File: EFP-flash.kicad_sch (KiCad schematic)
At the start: 17 parts, among them J101 USB_C_Receptacle_USB2.0, J102 Conn_01x06, Q101 MMDT3904, SW101 SW_SPDT, U101 ESD PROTECTION, U102 TLV75533PDBV, U103 CH340C

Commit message: PCB complete
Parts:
- added D102: GREEN, LED_SMD:LED_0603_1608Metric, symbol Device:LED
- added J101: USB_B_Micro, Connector_USB_custom:USB_Micro-B_Amphenol_10118194_Horizontal, symbol Connector:USB_B_Micro
- added LOGO101: Open_Hardware, Symbol:OSHW-Logo2_7.3x6mm_SilkScreen, symbol Graphic:Logo_Open_Hardware_Large
- added R105: 10kΩ, Resistor_SMD:R_0603_1608Metric, symbol Device:R_Small_US
- J103: renamed from J102; JLCPCB_IGNORE (none) -> 1
- U101: JLCPCB_CORRECTION (none) -> 0;0;180
- U102: JLCPCB_CORRECTION (none) -> 0;0;180; LCSC C255621 C404027 -> C404027
- renumbered J101 to J102
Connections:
- net 3v3_{SW}: now also D102.2 (A)
- net GND: now also J101.5 (GND), J101.6 (Shield), R105.2
- net SER_RX: now also J103.2 (Pin_2); no longer J103.3 (Pin_3)
- net SER_TX: now also J103.3 (Pin_3); no longer J103.2 (Pin_2)
- net USB_D+: now also U101.1 (I/O1), J101.3 (D+); no longer U101.6 (I/O4)
- net USB_D-: now also U101.6 (I/O4), J101.2 (D-); no longer U101.1 (I/O1)
- net at F101.2, J102.A4 (VBUS), J102.A9 (VBUS)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: now also J101.1 (VBUS)
- new net: D102.1 (K), R105.1
- no-connect marks 10 -> 11
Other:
- note added: "Gnd Rx Tx 3v3 EN Boot"
- note removed: "Gnd Tx Rx 3v3 EN Boot"
- moved on the sheet: SW101

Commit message: Sent to board fab v1.0.1, replaces previous
Changes:
 - USB diodes out of stock; different manufacturer had their stock.
 - SPDT switch out of stock, replaced with a different switch that
   thankfully also had a footprint in KiCAD
 - Made the board slightly wider to accomodate the switch.
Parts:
- SW101: footprint Button_Switch_SMD:SW_SPDT_PCM12 -> Button_Switch_SMD:SW_SPDT_CK-JS102011SAQN; JLCPCB_CORRECTION (none) -> 0;-2.75;180; LCSC C109335 -> C125040
- U102: LCSC C404027 -> C2937042
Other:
- company: (none) -> OSH
- title: (none) -> ESP-Flash
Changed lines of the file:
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@@
 (kicad_sch (version 20211123) (generator eeschema)
   (paper "A4")
+  (title_block
+    (title "ESP-Flash")
+    (date "2023-01-03")
+    (rev "v1.1.0")
+    (company "OSH")
+    (comment 1 "Drawn by: VGD")
+  )
   (junction (at 82.55 101.6) (diameter 0) (color 0 0 0 0)
   )
@@
       (effects (font (size 1.27 1.27)) hide)
     )
+    (pin "1")
+    (pin "2")
+    (pin "6")
     (pin "3")
     (pin "4")
@@
     (property "Reference" "SW101" (id 0) (at 213.36 64.77 0))
     (property "Value" "SW_SPDT" (id 1) (at 213.36 67.31 0))
-    (property "Footprint" "Button_Switch_SMD:SW_SPDT_PCM12" (id 2) (at 213.36 72.39 0)
+    (property "Footprint" "Button_Switch_SMD:SW_SPDT_CK-JS102011SAQN" (id 2) (at 213.36 72.39 0)
       (effects (font (size 1.27 1.27)) hide)
     )
@@
       (effects (font (size 1.27 1.27)) hide)
     )
-    (property "LCSC" "C109335" (id 4) (at 213.36 72.39 0)
+    (property "LCSC" "C125040" (id 4) (at 213.36 72.39 0)
+      (effects (font (size 1.27 1.27)) hide)
+    )
+    (property "JLCPCB_CORRECTION" "0;-2.75;180" (id 5) (at 213.36 72.39 0)
       (effects (font (size 1.27 1.27)) hide)
     )
@@
     (pin "2")
     (pin "6")
+    (pin "3")
+    (pin "4")
+    (pin "5")
   )
   (symbol (lib_id "Device:R_US") (at 71.12 113.03 180) (unit 1)
@@
       (effects (font (size 1.27 1.27)) hide)
     )
-    (property "LCSC" "C404027" (id 4) (at 115.57 40.64 0)
+    (property "LCSC" "C2937042" (id 4) (at 115.57 40.64 0)
       (effects (font (size 1.27 1.27)) hide)
     )
@@
     )
     (path "/7fed758a-c76e-4f1a-8799-89d9d2a905c1"
-      (reference "SW101") (unit 1) (value "SW_SPDT") (footprint "Button_Switch_SMD:SW_SPDT_PCM12")
+      (reference "SW101") (unit 1) (value "SW_SPDT") (footprint "Button_Switch_SMD:SW_SPDT_CK-JS102011SAQN")
     )
     (path "/e1bad162-1779-40d0-8d1a-a95bb6a2350e"

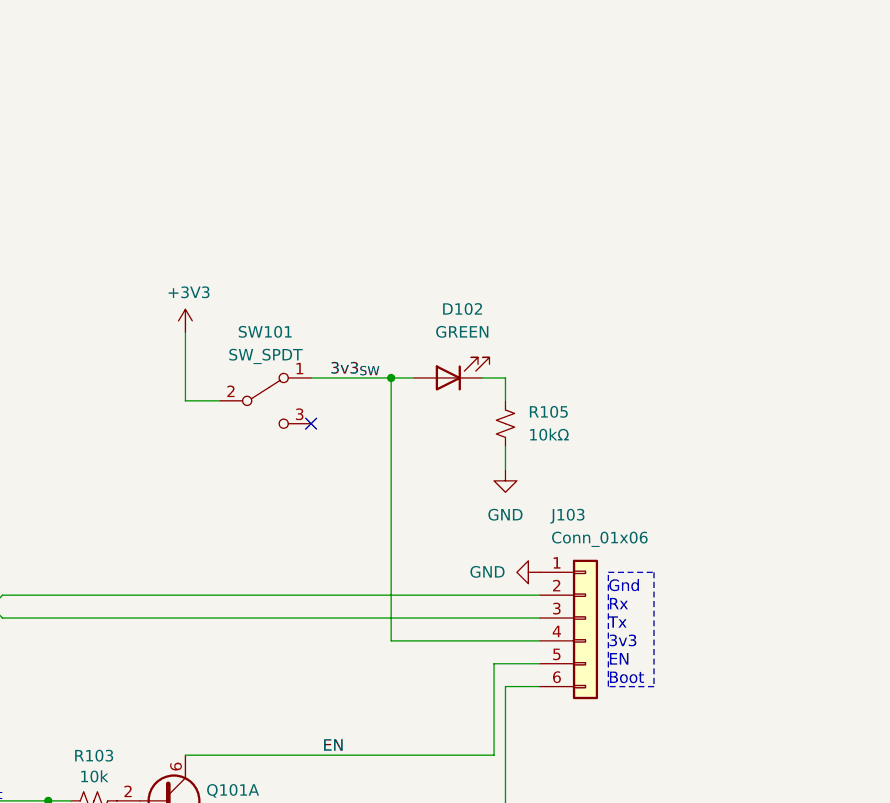
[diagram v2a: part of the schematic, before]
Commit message: Bugfix: PWR LED backfed from board
Power LED would light up when board was using its own 3v3 Power, even
though the switch was in the off position.

Found a clever solution to fix this, by changing two short traces.
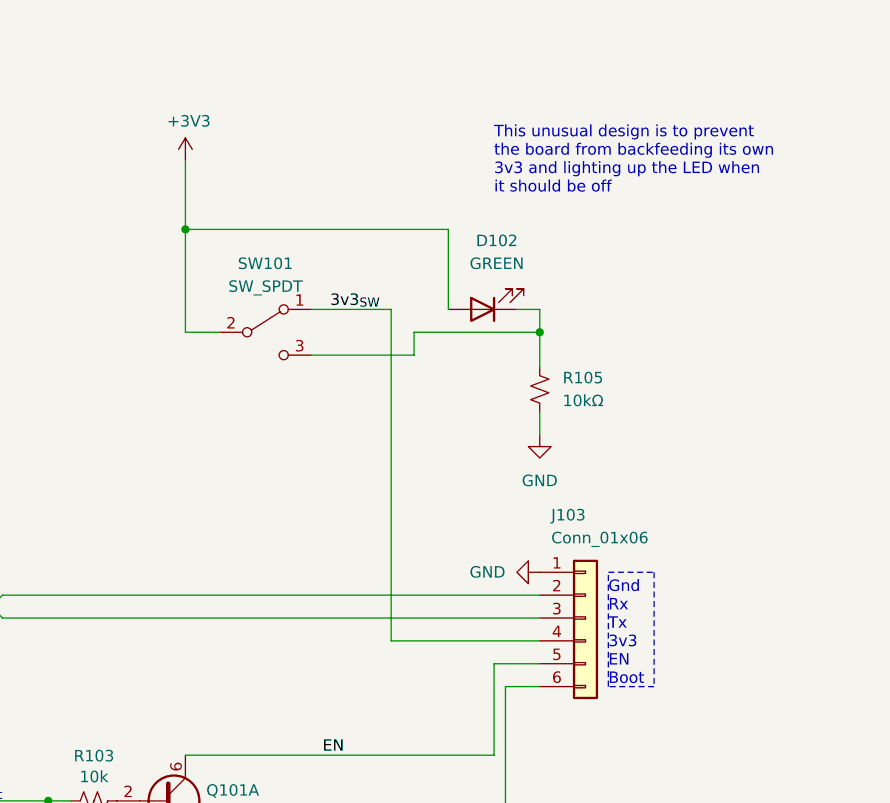
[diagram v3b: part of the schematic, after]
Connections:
- net +3V3: now also D102.2 (A)
- net 3v3_{SW}: no longer D102.2 (A)
- net at D102.1 (K), R105.1: now also SW101.3 (C)
- no-connect marks 11 -> 10
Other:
- note added: "This unusual design is to prevent the board from backfeeding its own 3v3 and lighting up the LED when it should be off"
- moved on the sheet: D102, R105, SW101

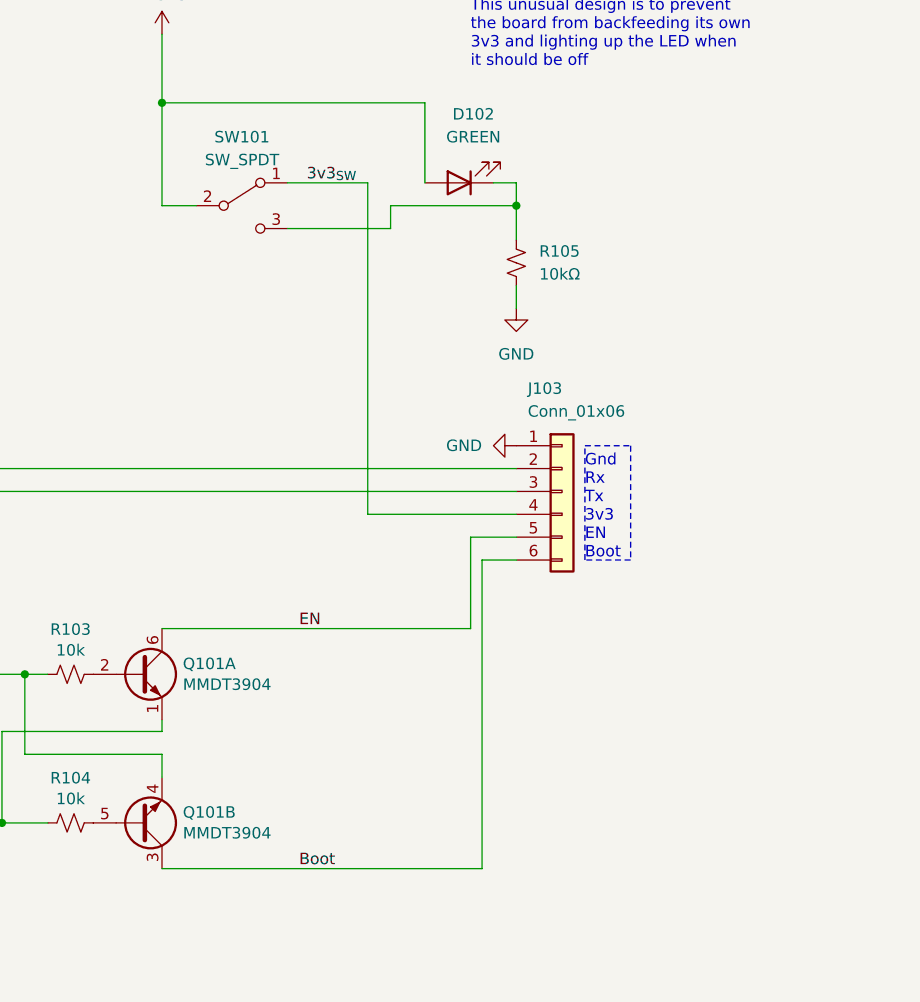
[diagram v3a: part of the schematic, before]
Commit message: Add 2nd indicator LED
- The first one is linked to the switch, and indicates when the switch
  is closed, linking the 3v3 nets together.
- The second one is linked directly to the 3v3 pin on the programmer. It
  will also turn on when the target board has its own power source.
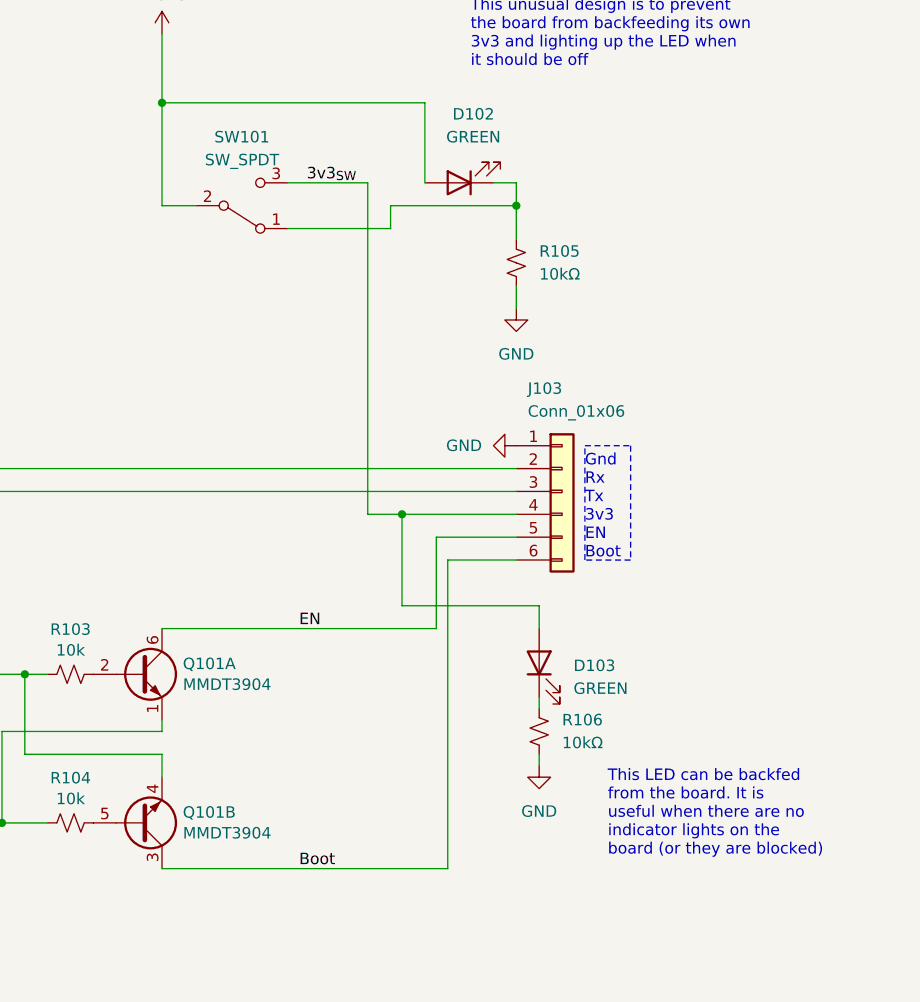
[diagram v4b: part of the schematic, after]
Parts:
- added D103: GREEN, LED_SMD:LED_0603_1608Metric, symbol Device:LED
- added R106: 10kΩ, Resistor_SMD:R_0603_1608Metric, symbol Device:R_Small_US
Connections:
- net 3v3_{SW}: now also SW101.3 (C), D103.2 (A); no longer SW101.1 (A)
- net GND: now also R106.2
- net at D102.1 (K), R105.1: now also SW101.1 (A); no longer SW101.3 (C)
- new net: D103.1 (K), R106.1
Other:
- note added: "This LED can be backfed from the board. It is useful when there are no indicator lights on the board (or they are blocked)"
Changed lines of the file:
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@@
   (junction (at 106.68 38.1) (diameter 0) (color 0 0 0 0)
+  )
+  (junction (at 231.14 99.06) (diameter 0) (color 0 0 0 0)
   )
   (junction (at 189.23 116.84) (diameter 0) (color 0 0 0 0)
@@
     (stroke (width 0) (type default) (color 0 0 0 0))
   )
+  (wire (pts (xy 246.38 119.38) (xy 246.38 120.65))
+    (stroke (width 0) (type default) (color 0 0 0 0))
+  )
   (wire (pts (xy 77.47 101.6) (xy 74.93 104.14))
     (stroke (width 0) (type default) (color 0 0 0 0))
@@
     (stroke (width 0) (type default) (color 0 0 0 0))
   )
+  (wire (pts (xy 227.33 99.06) (xy 231.14 99.06))
+    (stroke (width 0) (type default) (color 0 0 0 0))
+  )
   (wire (pts (xy 77.47 104.14) (xy 74.93 101.6))
     (stroke (width 0) (type default) (color 0 0 0 0))
@@
     (stroke (width 0) (type default) (color 0 0 0 0))
   )
+  (wire (pts (xy 231.14 109.22) (xy 231.14 99.06))
+    (stroke (width 0) (type default) (color 0 0 0 0))
+  )
   (wire (pts (xy 125.73 38.1) (xy 137.16 38.1))
     (stroke (width 0) (type default) (color 0 0 0 0))
@@
     (stroke (width 0) (type default) (color 0 0 0 0))
   )
+  (wire (pts (xy 231.14 99.06) (xy 243.84 99.06))
+    (stroke (width 0) (type default) (color 0 0 0 0))
+  )
   (wire (pts (xy 243.84 73.66) (xy 243.84 76.2))
     (stroke (width 0) (type solid) (color 0 0 0 0))
@@
     (stroke (width 0) (type default) (color 0 0 0 0))
   )
+  (wire (pts (xy 246.38 109.22) (xy 231.14 109.22))
+    (stroke (width 0) (type default) (color 0 0 0 0))
+  )
   (wire (pts (xy 204.47 125.73) (xy 204.47 128.27))
     (stroke (width 0) (type default) (color 0 0 0 0))
@@
     (stroke (width 0) (type default) (color 0 0 0 0))
   )
-  (wire (pts (xy 238.76 101.6) (xy 243.84 101.6))
+  (wire (pts (xy 234.95 101.6) (xy 243.84 101.6))
     (stroke (width 0) (type default) (color 0 0 0 0))
   )
@@
     (stroke (width 0) (type default) (color 0 0 0 0))
   )
-  (wire (pts (xy 238.76 111.76) (xy 238.76 101.6))
+  (wire (pts (xy 234.95 111.76) (xy 234.95 101.6))
     (stroke (width 0) (type default) (color 0 0 0 0))
   )
@@
     (stroke (width 0) (type default) (color 0 0 0 0))
   )
-  (wire (pts (xy 240.03 104.14) (xy 243.84 104.14))
+  (wire (pts (xy 236.22 104.14) (xy 243.84 104.14))
     (stroke (width 0) (type default) (color 0 0 0 0))
   )
@@
     (stroke (width 0) (type default) (color 0 0 0 0))
   )
+  (wire (pts (xy 246.38 111.76) (xy 246.38 109.22))
+    (stroke (width 0) (type default) (color 0 0 0 0))
+  )
   (wire (pts (xy 189.23 116.84) (xy 189.23 125.73))
     (stroke (width 0) (type default) (color 0 0 0 0))
@@
     (stroke (width 0) (type default) (color 0 0 0 0))
   )
-  (wire (pts (xy 204.47 111.76) (xy 238.76 111.76))
+  (wire (pts (xy 204.47 111.76) (xy 234.95 111.76))
     (stroke (width 0) (type default) (color 0 0 0 0))
   )
@@
   (wire (pts (xy 233.68 53.34) (xy 233.68 62.23))
     (stroke (width 0) (type default) (color 0 0 0 0))
+  )
+  (wire (pts (xy 246.38 125.73) (xy 246.38 127))
+    (stroke (width 0) (type solid) (color 0 0 0 0))
   )
   (wire (pts (xy 52.07 101.6) (xy 54.61 101.6))
@@
     (stroke (width 0) (type solid) (color 0 0 0 0))
   )
-  (wire (pts (xy 227.33 99.06) (xy 243.84 99.06))
-    (stroke (width 0) (type default) (color 0 0 0 0))
-  )
   (wire (pts (xy 74.93 101.6) (xy 54.61 101.6))
     (stroke (width 0) (type default) (color 0 0 0 0))
@@
     (stroke (width 0) (type default) (color 0 0 0 0))
   )
-  (wire (pts (xy 240.03 138.43) (xy 240.03 104.14))
+  (wire (pts (xy 236.22 138.43) (xy 236.22 104.14))
     (stroke (width 0) (type default) (color 0 0 0 0))
   )
@@
     (stroke (width 0) (type default) (color 0 0 0 0))
   )
-  (wire (pts (xy 204.47 138.43) (xy 240.03 138.43))
+  (wire (pts (xy 204.47 138.43) (xy 236.22 138.43))
     (stroke (width 0) (type default) (color 0 0 0 0))
   )
@@
   (text "This unusual design is to prevent\nthe board from backfeeding its own\n3v3 and lighting up the LED when\nit should be off"
     (at 238.76 49.53 0)
+    (effects (font (size 1.27 1.27)) (justify left bottom))
+  )
+  (text "This LED can be backfed\nfrom the board. It is\nuseful when there are no\nindicator lights on the\nboard (or they are blocked)"
+    (at 254 137.16 0)
     (effects (font (size 1.27 1.27)) (justify left bottom))
   )
@@
     (pin "6")
   )
+  (symbol (lib_id "Device:LED") (at 246.38 115.57 90) (unit 1)
+    (in_bom yes) (on_board yes) (fields_autoplaced)
+    (property "Reference" "D103" (id 0) (at 250.19 115.8874 90)
+      (effects (font (size 1.27 1.27)) (justify right))
+    )
+    (property "Value" "GREEN" (id 1) (at 250.19 118.4274 90)
+      (effects (font (size 1.27 1.27)) (justify right))
+    )
+    (property "Footprint" "LED_SMD:LED_0603_1608Metric" (id 2) (at 246.38 115.57 0)
+      (effects (font (size 1.27 1.27)) hide)
+    )
+    (property "Datasheet" "~" (id 3) (at 246.38 115.57 0)
+      (effects (font (size 1.27 1.27)) hide)
+    )
+    (property "LCSC" "C72043" (id 4) (at 246.38 115.57 0)
+      (effects (font (size 1.27 1.27)) hide)
+    )
+    (pin "1")
+    (pin "2")
+  )
   (symbol (lib_id "Device:Polyfuse") (at 68.58 72.39 270) (unit 1)
     (in_bom yes) (on_board yes)
@@
     (pin "2")
   )
+  (symbol (lib_id "power:GND") (at 246.38 127 0) (unit 1)
+    (in_bom yes) (on_board yes) (fields_autoplaced)
+    (property "Reference" "#PWR0119" (id 0) (at 246.38 133.35 0)
+      (effects (font (size 1.27 1.27)) hide)
+    )
+    (property "Value" "GND" (id 1) (at 246.38 132.08 0))
+    (property "Footprint" "" (id 2) (at 246.38 127 0)
+      (effects (font (size 1.27 1.27)) hide)
+    )
+    (property "Datasheet" "" (id 3) (at 246.38 127 0)
+      (effects (font (size 1.27 1.27)) hide)
+    )
+    (pin "1")
+  )
   (symbol (lib_id "power:GND") (at 115.57 48.26 0) (unit 1)
     (in_bom yes) (on_board yes)
@@
     )
     (pin "1")
+  )
+  (symbol (lib_id "Device:R_Small_US") (at 246.38 123.19 0) (unit 1)
+    (in_bom yes) (on_board yes) (fields_autoplaced)
+    (property "Reference" "R106" (id 0) (at 248.92 121.9199 0)
+      (effects (font (size 1.27 1.27)) (justify left))
+    )
+    (property "Value" "10kΩ" (id 1) (at 248.92 124.4599 0)
+      (effects (font (size 1.27 1.27)) (justify left))
+    )
+    (property "Footprint" "Resistor_SMD:R_0603_1608Metric" (id 2) (at 246.38 123.19 0)
+      (effects (font (size 1.27 1.27)) hide)
+    )
+    (property "Datasheet" "~" (id 3) (at 246.38 123.19 0)
+      (effects (font (size 1.27 1.27)) hide)
+    )
+    (property "LCSC" "C25804" (id 4) (at 246.38 123.19 0)
+      (effects (font (size 1.27 1.27)) hide)
+    )
+    (pin "1")
+    (pin "2")
   )
   (symbol (lib_id "power:PWR_FLAG") (at 76.2 72.39 180) (unit 1)
@@
       (effects (font (size 1.27 1.27)) hide)
     )
-    (pin "1")
-    (pin "2")
-    (pin "6")
     (pin "3")
     (pin "4")
@@
     (pin "2")
   )
-  (symbol (lib_id "Switch:SW_SPDT") (at 213.36 64.77 0) (unit 1)
+  (symbol (lib_id "Switch:SW_SPDT") (at 213.36 64.77 0) (mirror x) (unit 1)
     (in_bom yes) (on_board yes) (fields_autoplaced)
     (property "Reference" "SW101" (id 0) (at 213.36 57.15 0))
@@
     (pin "2")
     (pin "6")
-    (pin "3")
-    (pin "4")
-    (pin "5")
   )
   (symbol (lib_id "Device:R_US") (at 71.12 113.03 180) (unit 1)
@@
       (reference "#PWR0118") (unit 1) (value "GND") (footprint "")
     )
+    (path "/3ee0d96a-e643-4ad1-b648-5d21c1a0d764"
+      (reference "#PWR0119") (unit 1) (value "GND") (footprint "")
+    )
     (path "/be7ac166-be14-487f-8122-b6677f912163"
       (reference "C101") (unit 1) (value "1uF/10V") (footprint "Capacitor_SMD:C_0805_2012Metric")
@@
       (reference "D102") (unit 1) (value "GREEN") (footprint "LED_SMD:LED_0603_1608Metric")
     )
+    (path "/28cd7b49-5d04-4ad2-8783-b564b725e09e"
+      (reference "D103") (unit 1) (value "GREEN") (footprint "LED_SMD:LED_0603_1608Metric")
+    )
     (path "/32198c43-7669-4448-8c2e-012135c9a81c"
       (reference "F101") (unit 1) (value "0ZCK0050FF2E (TLC-PSMD050)") (footprint "Fuse:Fuse_0805_2012Metric_Pad1.15x1.40mm_HandSolder")
@@
       (reference "R105") (unit 1) (value "10kΩ") (footprint "Resistor_SMD:R_0603_1608Metric")
     )
+    (path "/429c92a6-4d68-4597-8844-fc88f311c899"
+      (reference "R106") (unit 1) (value "10kΩ") (footprint "Resistor_SMD:R_0603_1608Metric")
+    )
     (path "/7fed758a-c76e-4f1a-8799-89d9d2a905c1"

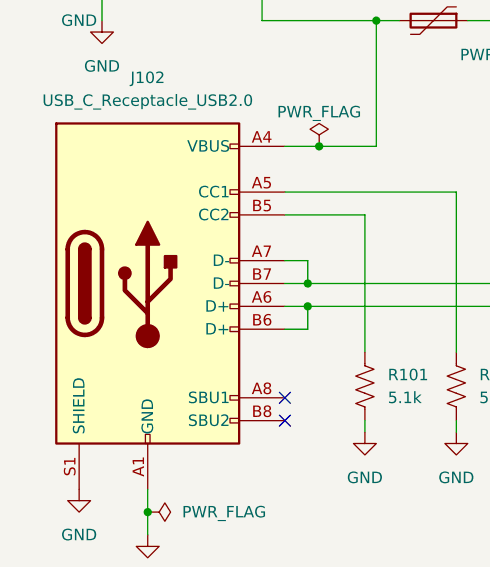
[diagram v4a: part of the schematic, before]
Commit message: Convert to 7.0 format, fix DRC errors
Opened and saved with KiCAD 7.0

Fix a few unconnected components. Adjusted DRC violation severities to
ignore silkscreen over board edge (because they're usually on purpose
and don't help track down errors).
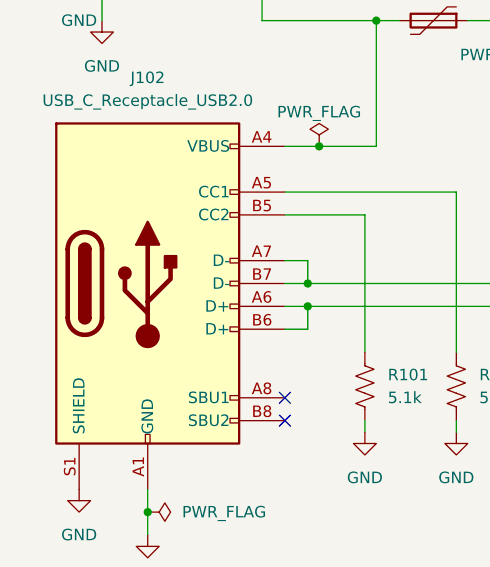
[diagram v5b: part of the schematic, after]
